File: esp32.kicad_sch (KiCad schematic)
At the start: 25 parts, among them J2 TC2030-IDC, J3 Conn_01x04, J4 USB_C_Receptacle_USB2.0, SW1 GT-TC029B-H025-L1N, SW2 GT-TC029B-H025-L1N, U7 RT9080-33GJ5, U8 ESP32-S3-WROOM-1, Y1 32.768kHz

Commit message: adding logo and docs
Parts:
- C18: DK 1276-1096-1-ND -> 399-C0805C106K8PAC7800DKR-ND; PARTNO CL21A106KOQNNNE -> C0805C106K8PAC7800
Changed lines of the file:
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@@
       (effects (font (size 1.27 1.27)) hide)
     )
-    (property "DK" "1276-1096-1-ND" (at 130.81 60.325 0)
+    (property "DK" "399-C0805C106K8PAC7800DKR-ND" (at 130.81 60.325 0)
       (effects (font (size 1.27 1.27)) hide)
     )
-    (property "PARTNO" "CL21A106KOQNNNE" (at 130.81 60.325 0)
+    (property "PARTNO" "C0805C106K8PAC7800" (at 130.81 60.325 0)
       (effects (font (size 1.27 1.27)) hide)
     )

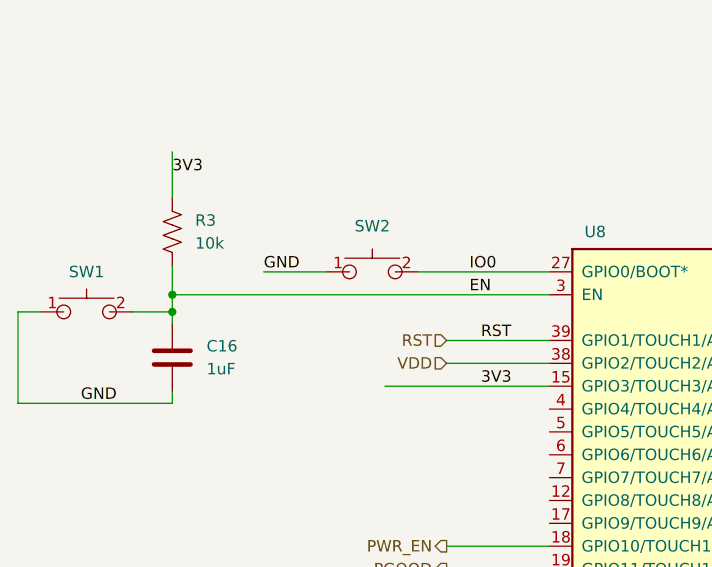
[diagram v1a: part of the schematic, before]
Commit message: migrated over lots of bitaxe parts to blockaxe
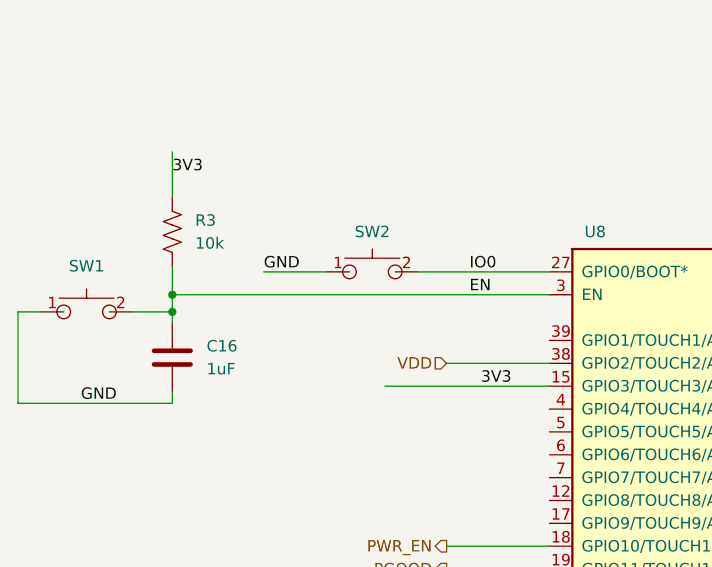
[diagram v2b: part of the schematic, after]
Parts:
- J2: footprint bitaxe:Tag-Connect_TC2030-IDC-NL_2x03_P1.27mm_Vertical -> blockaxe:Tag-Connect_TC2030-IDC-NL_2x03_P1.27mm_Vertical; symbol bitaxe:TC2030-IDC-NL -> blockaxe:TC2030-IDC-NL; now in the parts list
- SW1, SW2: footprint bitaxe:SW_CS1213AGF260_CRS -> blockaxe:SW_CS1213AGF260_CRS; symbol bitaxe:GT-TC029B-H025-L1N -> blockaxe:GT-TC029B-H025-L1N
- U8: footprint bitaxe:ESP32-S3-WROOM-1 -> blockaxe:ESP32-S3-WROOM-1; symbol bitaxe:ESP32-S3-WROOM-1 -> blockaxe:ESP32-S3-WROOM-1
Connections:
- net RST: no longer names the net of U8.39 (GPIO1/TOUCH1/ADC1_CH0)
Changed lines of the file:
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@@
-    (stroke (width 0) (type default))
-  )
-  (wire (pts (xy 86.36 83.185) (xy 74.93 83.185))
     (stroke (width 0) (type default))
   )
@@
   )
   (label "3V3" (at 193.802 30.48 0) (fields_autoplaced)
-    (effects (font (size 1.27 1.27)) (justify left bottom))
-  )
-  (label "RST" (at 78.74 83.185 0) (fields_autoplaced)
     (effects (font (size 1.27 1.27)) (justify left bottom))
   )
@@
     )
   )
-  (hierarchical_label "RST" (shape input) (at 74.93 83.185 180) (fields_autoplaced)
-    (effects (font (size 1.27 1.27)) (justify right))
-  )
   (hierarchical_label "RX" (shape input) (at 74.93 126.365 180) (fields_autoplaced)
     (effects (font (size 1.27 1.27)) (justify right))
@@
     )
   )
-  (symbol (lib_id "bitaxe:GT-TC029B-H025-L1N") (at 66.675 75.565 0) (unit 1)
+  (symbol (lib_id "blockaxe:GT-TC029B-H025-L1N") (at 66.675 75.565 0) (unit 1)
     (in_bom yes) (on_board yes) (dnp no) (fields_autoplaced)
-    (property "Reference" "SW2" (at 66.675 70.485 0)
+    (property "Reference" "SW2" (at 66.675 71.12 0)
       (effects (font (size 1.27 1.27)))
     )
@@
       (effects (font (size 1.27 1.27)) hide)
     )
-    (property "Footprint" "bitaxe:SW_CS1213AGF260_CRS" (at 66.675 83.185 0)
+    (property "Footprint" "blockaxe:SW_CS1213AGF260_CRS" (at 66.675 83.185 0)
       (effects (font (size 1.27 1.27)) hide)
     )
@@
     )
   )
-  (symbol (lib_id "bitaxe:ESP32-S3-WROOM-1") (at 142.24 106.045 0) (unit 1)
+  (symbol (lib_id "blockaxe:ESP32-S3-WROOM-1") (at 142.24 106.045 0) (unit 1)
     (in_bom yes) (on_board yes) (dnp no)
     (property "Reference" "U8" (at 91.44 71.12 0)
@@
       (effects (font (size 1.27 1.27)))
     )
-    (property "Footprint" "bitaxe:ESP32-S3-WROOM-1" (at 142.24 139.065 0)
+    (property "Footprint" "blockaxe:ESP32-S3-WROOM-1" (at 142.24 139.065 0)
       (effects (font (size 1.27 1.27)) hide)
     )
@@
     )
   )
-  (symbol (lib_id "bitaxe:TC2030-IDC-NL") (at 74.93 166.37 0) (unit 1)
-    (in_bom no) (on_board yes) (dnp no) (fields_autoplaced)
+  (symbol (lib_id "blockaxe:TC2030-IDC-NL") (at 74.93 166.37 0) (unit 1)
+    (in_bom yes) (on_board yes) (dnp no) (fields_autoplaced)
     (property "Reference" "J2" (at 74.93 153.67 0)
       (effects (font (size 1.27 1.27)))
@@
       (effects (font (size 1.27 1.27)))
     )
-    (property "Footprint" "bitaxe:Tag-Connect_TC2030-IDC-NL_2x03_P1.27mm_Vertical" (at 73.66 166.37 0)
+    (property "Footprint" "blockaxe:Tag-Connect_TC2030-IDC-NL_2x03_P1.27mm_Vertical" (at 73.66 166.37 0)
       (effects (font (size 1.27 1.27)) hide)
     )
@@
     )
   )
-  (symbol (lib_id "bitaxe:GT-TC029B-H025-L1N") (at 34.925 80.01 0) (unit 1)
+  (symbol (lib_id "blockaxe:GT-TC029B-H025-L1N") (at 34.925 80.01 0) (unit 1)
     (in_bom yes) (on_board yes) (dnp no) (fields_autoplaced)
-    (property "Reference" "SW1" (at 34.925 75.565 0)
+    (property "Reference" "SW1" (at 34.925 74.93 0)
       (effects (font (size 1.27 1.27)))
     )
@@
       (effects (font (size 1.27 1.27)) hide)
     )
-    (property "Footprint" "bitaxe:SW_CS1213AGF260_CRS" (at 34.925 87.63 0)
-      (effects (font (size 1.27 1.27)) hide)
-    )
+    (property "Footprint" "blockaxe:SW_CS1213AGF260_CRS" (at 34.925 87.63 0)
+      (effects (font (size 1.27 1.27)) hide)
+    )

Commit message: all the footprints are in?
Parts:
- U7: footprint bitaxe:RT9080-33GJ5 -> blockaxe:RT9080-33GJ5
- Y1: footprint bitaxe:SC32S-7PF20PPM -> blockaxe:SC32S-7PF20PPM
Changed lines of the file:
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@@
       (effects (font (size 1.27 1.27)))
     )
-    (property "Footprint" "bitaxe:SC32S-7PF20PPM" (at 146.05 27.94 0)
+    (property "Footprint" "blockaxe:SC32S-7PF20PPM" (at 146.05 27.94 0)
       (effects (font (size 1.27 1.27)) hide)
     )
@@
       (effects (font (size 1.27 1.27)))
     )
-    (property "Footprint" "bitaxe:RT9080-33GJ5" (at 109.855 10.795 0)
+    (property "Footprint" "blockaxe:RT9080-33GJ5" (at 109.855 10.795 0)
       (effects (font (size 1.524 1.524)) hide)
     )

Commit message: more placing and routing
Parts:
- J3: footprint Connector_PinHeader_2.54mm:PinHeader_1x04_P2.54mm_Vertical -> Connector_PinSocket_2.54mm:PinSocket_1x04_P2.54mm_Vertical_SMD_Pin1Right; DK (none) -> NPTC041KFXC-RC
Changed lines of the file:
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@@
       (effects (font (size 1.27 1.27)) (justify left))
     )
-    (property "Footprint" "Connector_PinHeader_2.54mm:PinHeader_1x04_P2.54mm_Vertical" (at 205.74 30.48 0)
+    (property "Footprint" "Connector_PinSocket_2.54mm:PinSocket_1x04_P2.54mm_Vertical_SMD_Pin1Right" (at 205.74 30.48 0)
       (effects (font (size 1.27 1.27)) hide)
     )
@@
       (effects (font (size 1.27 1.27)) hide)
     )
+    (property "DK" "NPTC041KFXC-RC" (at 205.74 30.48 0)
+      (effects (font (size 1.27 1.27)) hide)
+    )

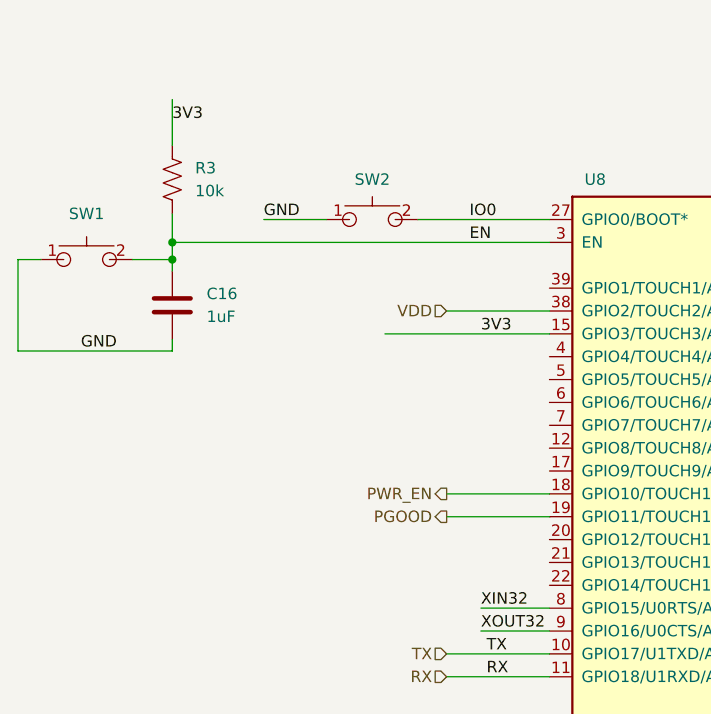
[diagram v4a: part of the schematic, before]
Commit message: more routing. switched to RA buttons, moved the buck closer to the barrel
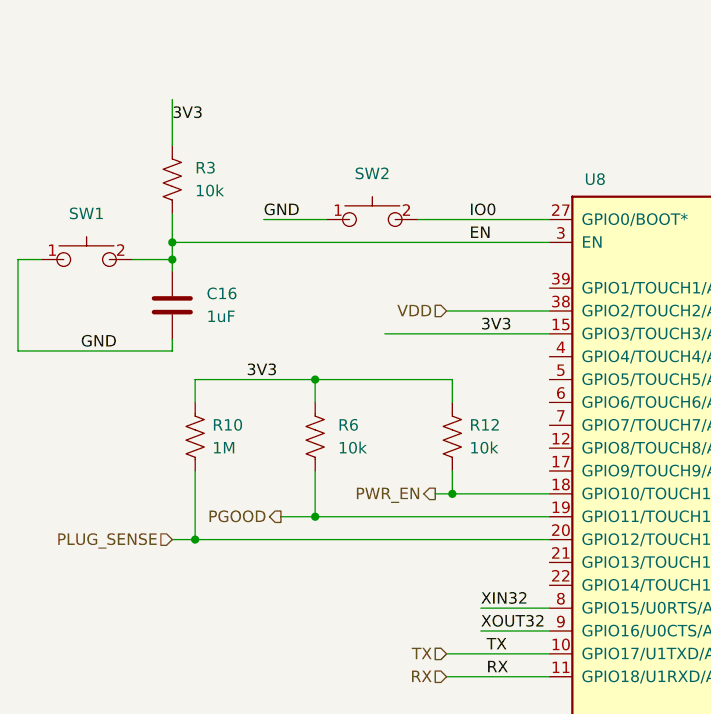
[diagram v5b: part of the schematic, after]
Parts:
- added R10: 1M, Resistor_SMD:R_0402_1005Metric, symbol Device:R_US
- added R12, R6: 10k, Resistor_SMD:R_0402_1005Metric, symbol Device:R_US
- SW1, SW2: value GT-TC029B-H025-L1N -> EVQ-9P701P; footprint blockaxe:SW_CS1213AGF260_CRS -> blockaxe:EVQ9P701P-switch; DK 2449-CS1213AGF260CT-ND -> P19095CT-ND; PARTNO CS1213AGF260 -> EVQ-9P701P
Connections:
- net 3V3: now also R10.1, R12.1, R6.1
- net PGOOD: now also R6.2
- net PWR_EN: now also R12.2
- net PLUG_SENSE: now reaches U8.20 (GPIO12/TOUCH12/ADC2_CH1/FSPICLK/FSPIIO6/SUBSPICLK)
- net PLUG_SENSE: now also R10.2

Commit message: finished routing. switched back to THT barrel
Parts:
- TP10, TP11, TP12, TP7, TP8, TP9: footprint TestPoint:TestPoint_Pad_D1.5mm -> TestPoint:TestPoint_Pad_D1.0mm
- renumbered Y1 to Y2
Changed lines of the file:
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@@
       (effects (font (size 1.27 1.27)) (justify left) hide)
     )
-    (property "Footprint" "TestPoint:TestPoint_Pad_D1.5mm" (at 74.93 139.065 0)
+    (property "Footprint" "TestPoint:TestPoint_Pad_D1.0mm" (at 74.93 139.065 0)
       (effects (font (size 1.27 1.27)) hide)
     )
@@
   (symbol (lib_id "Device:Crystal") (at 146.05 27.94 0) (unit 1)
     (in_bom yes) (on_board yes) (dnp no)
-    (property "Reference" "Y1" (at 146.05 20.955 0)
+    (property "Reference" "Y2" (at 146.05 20.955 0)
       (effects (font (size 1.27 1.27)))
     )
@@
       (project "blockaxe1"
         (path "/a166cb37-4e3a-4be5-b2da-277a3281a4de/97fce8a4-b016-4d76-8490-b8c988e88337"
-          (reference "Y1") (unit 1)
+          (reference "Y2") (unit 1)
         )
       )
@@
       (effects (font (size 1.27 1.27)) (justify left) hide)
     )
-    (property "Footprint" "TestPoint:TestPoint_Pad_D1.5mm" (at 60.325 168.91 0)
+    (property "Footprint" "TestPoint:TestPoint_Pad_D1.0mm" (at 60.325 168.91 0)
       (effects (font (size 1.27 1.27)) hide)
     )
@@
       (effects (font (size 1.27 1.27)) (justify left) hide)
     )
-    (property "Footprint" "TestPoint:TestPoint_Pad_D1.5mm" (at 74.93 142.24 0)
+    (property "Footprint" "TestPoint:TestPoint_Pad_D1.0mm" (at 74.93 142.24 0)
       (effects (font (size 1.27 1.27)) hide)
     )
@@
       (effects (font (size 1.27 1.27)) (justify left) hide)
     )
-    (property "Footprint" "TestPoint:TestPoint_Pad_D1.5mm" (at 88.9 163.83 0)
+    (property "Footprint" "TestPoint:TestPoint_Pad_D1.0mm" (at 88.9 163.83 0)
       (effects (font (size 1.27 1.27)) hide)
     )
@@
       (effects (font (size 1.27 1.27)) (justify left) hide)
     )
-    (property "Footprint" "TestPoint:TestPoint_Pad_D1.5mm" (at 60.325 171.45 0)
+    (property "Footprint" "TestPoint:TestPoint_Pad_D1.0mm" (at 60.325 171.45 0)
       (effects (font (size 1.27 1.27)) hide)
     )
@@
       (effects (font (size 1.27 1.27)) (justify left) hide)
     )
-    (property "Footprint" "TestPoint:TestPoint_Pad_D1.5mm" (at 60.325 173.99 0)
-      (effects (font (size 1.27 1.27)) hide)
-    )
+    (property "Footprint" "TestPoint:TestPoint_Pad_D1.0mm" (at 60.325 173.99 0)
+      (effects (font (size 1.27 1.27)) hide)
+    )

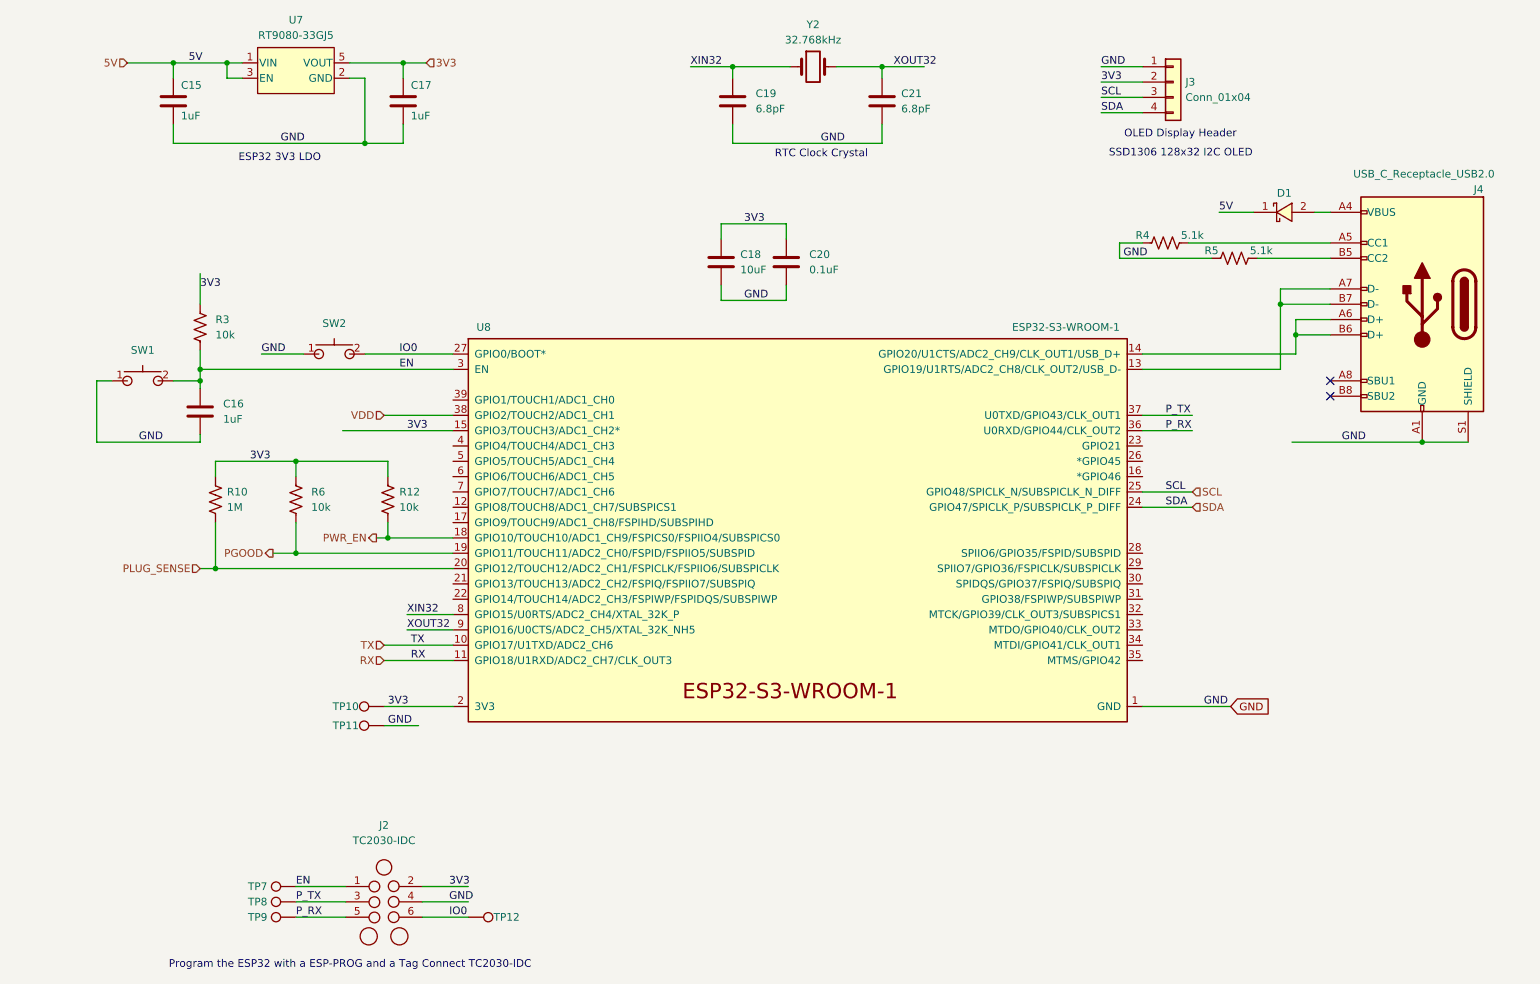
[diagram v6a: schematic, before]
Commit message: changed buttons for #5 flipped display for #2
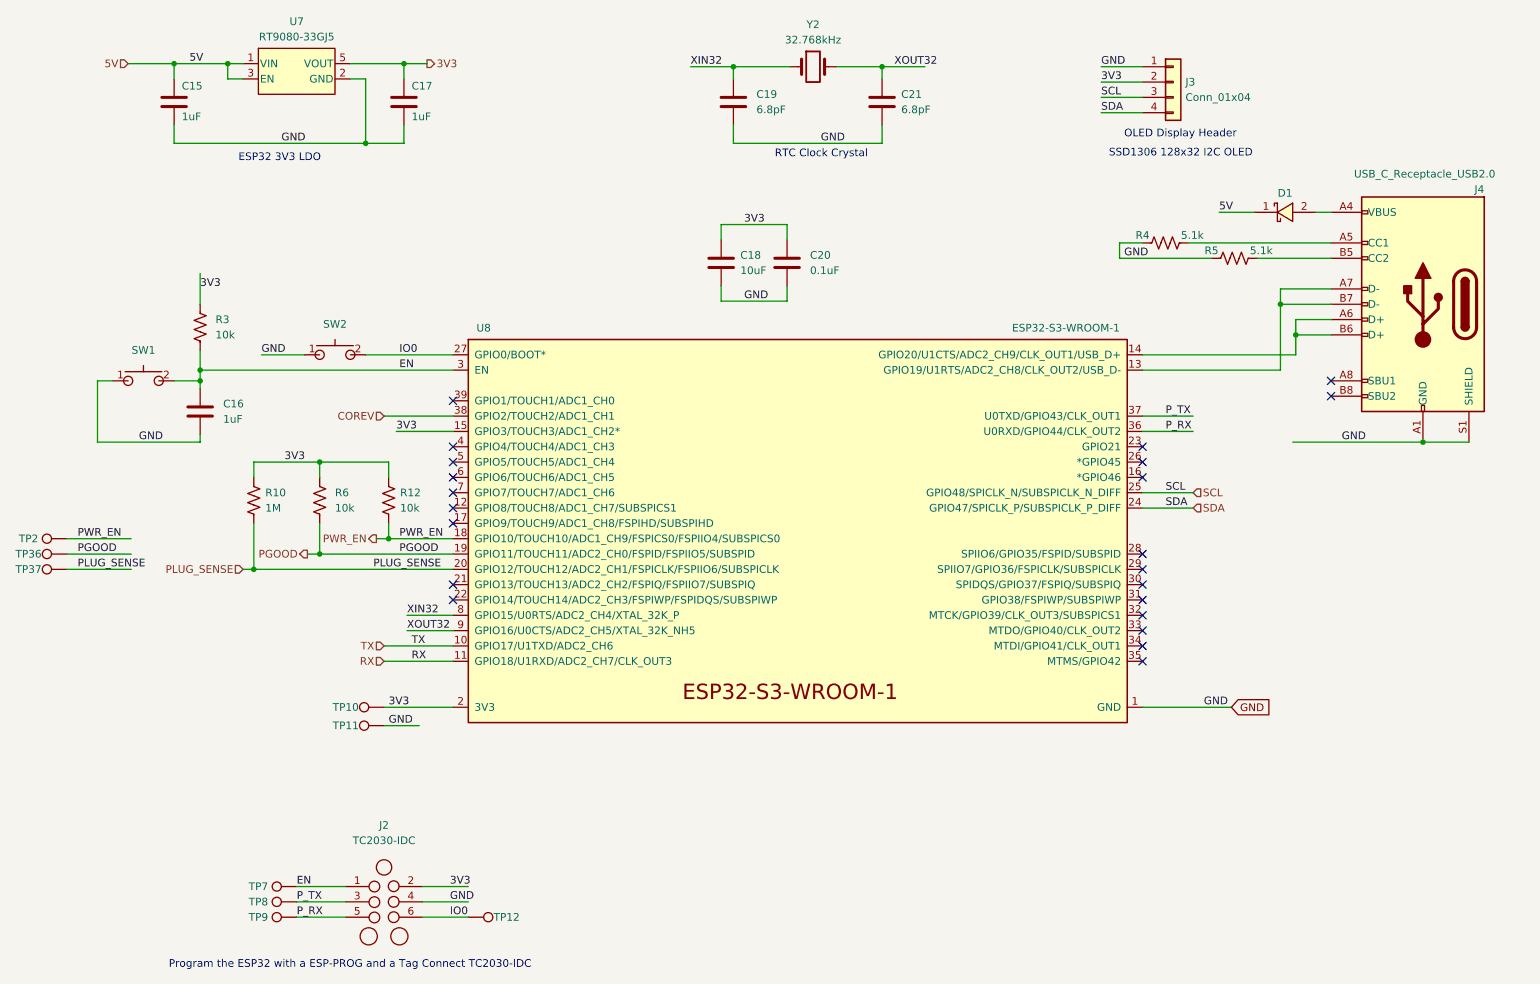
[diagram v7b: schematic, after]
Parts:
- added TP2, TP36, TP37: TestPoint, TestPoint:TestPoint_Pad_D1.0mm, symbol Connector:TestPoint
- SW1, SW2: value EVQ-9P701P -> TL3330AF260QG; footprint blockaxe:EVQ9P701P-switch -> blockaxe:SW_TL3330_EWI; DK P19095CT-ND -> EG4389CT-ND; PARTNO EVQ-9P701P -> TL3330AF260QG
- U7: symbol bitaxe:RT9080-33GJ5 -> blockaxe:RT9080-33GJ5
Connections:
- net PGOOD: now also TP36.1
- net PLUG_SENSE: now also TP37.1
- net PWR_EN: now also TP2.1
- net VDD renamed COREV
- no-connect marks 2 -> 22
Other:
- moved on the sheet: R10, R6
